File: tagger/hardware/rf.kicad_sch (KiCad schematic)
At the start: 13 parts, among them J3 RADIO_UART, SW1 RADIO_COMMISSION, U7 XB3-24Z8UM-J

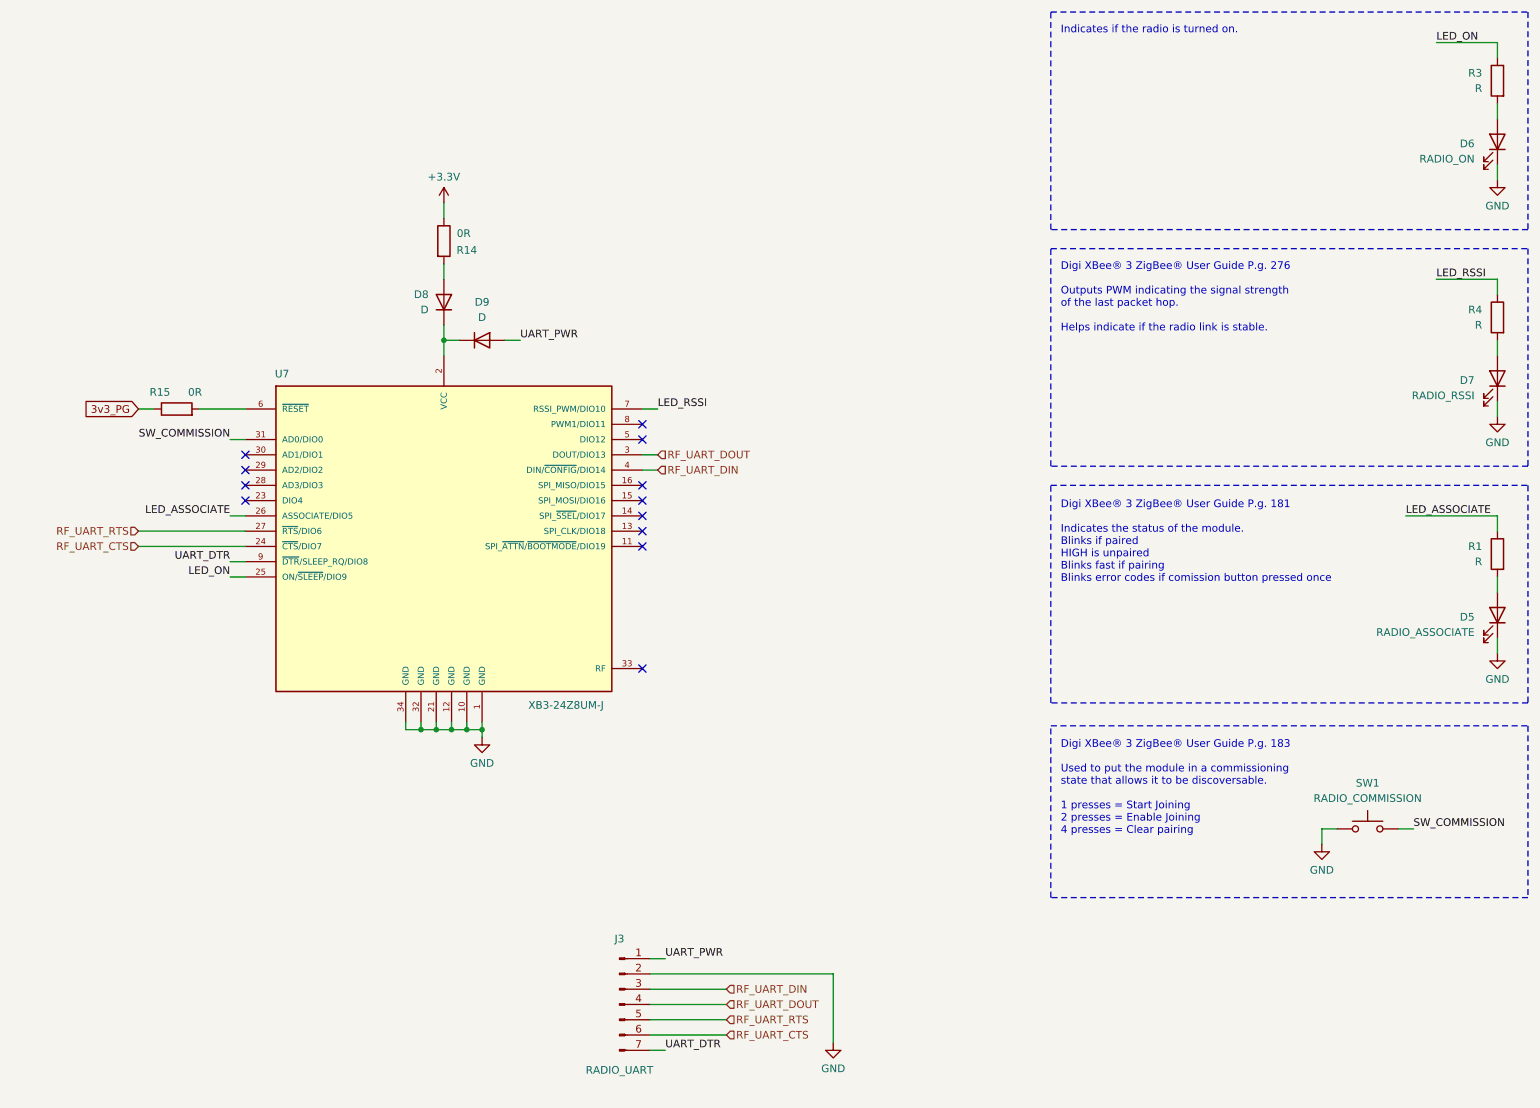
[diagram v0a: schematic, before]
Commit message: feat: schematic organization
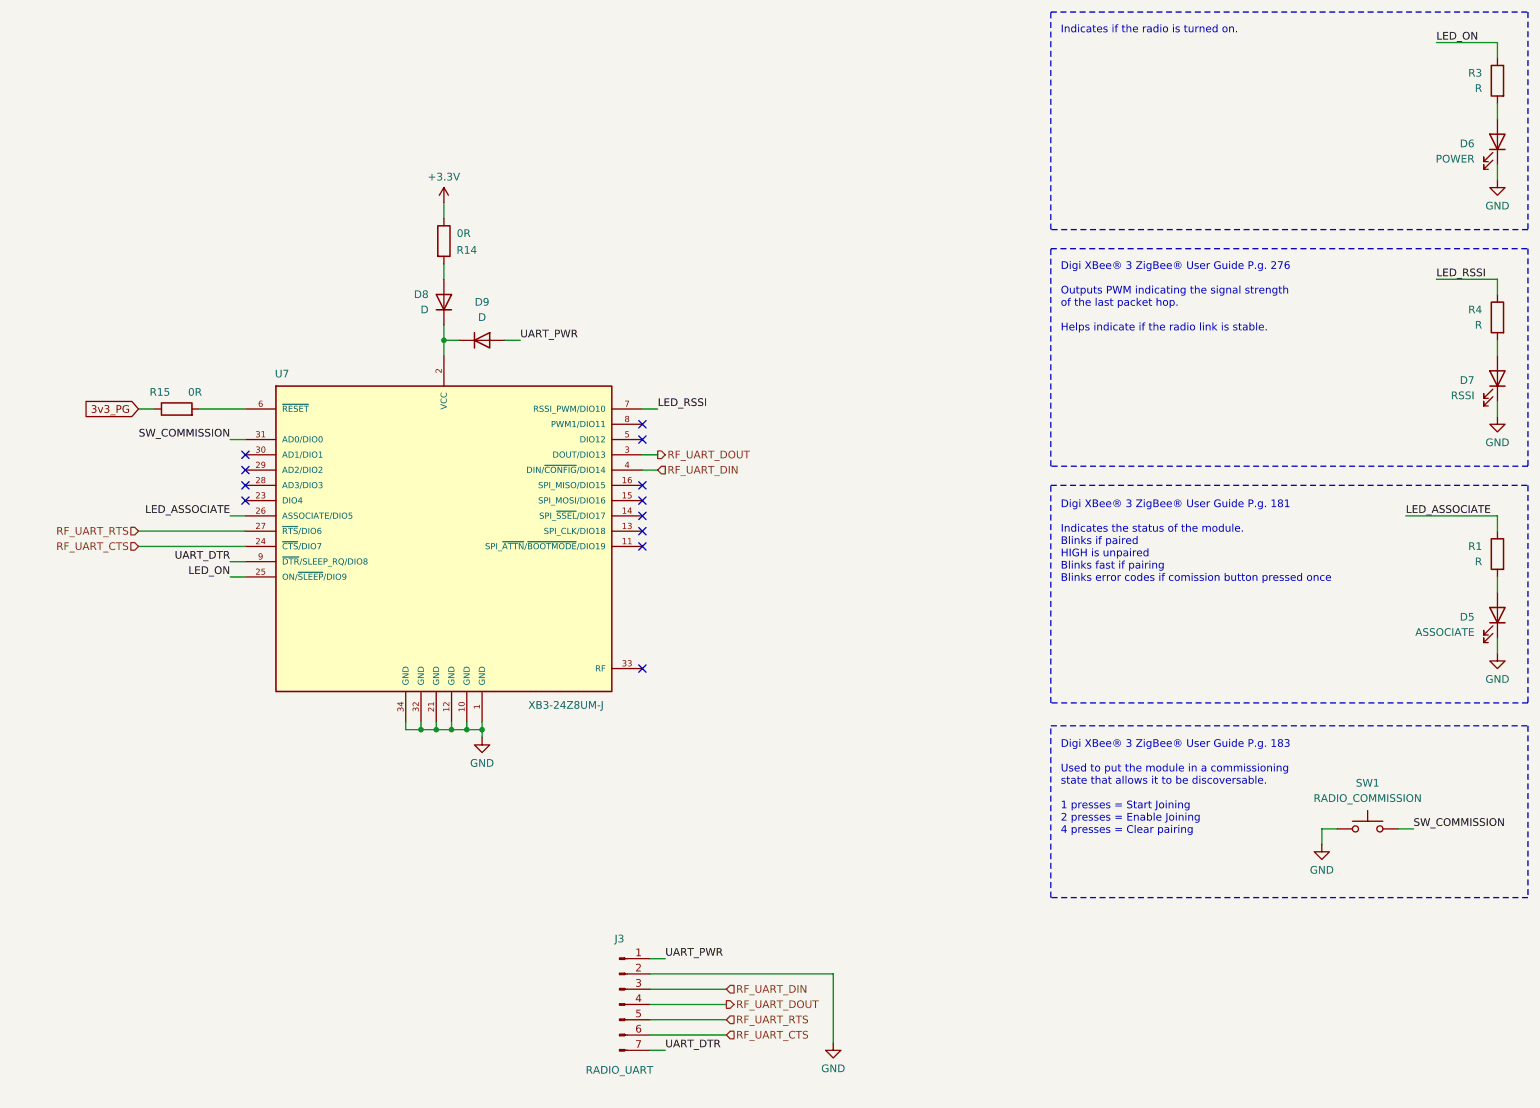
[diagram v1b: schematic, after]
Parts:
- D5: value RADIO_ASSOCIATE -> ASSOCIATE; footprint (none) -> LED_SMD:LED_0603_1608Metric
- D6: value RADIO_ON -> POWER; footprint (none) -> LED_SMD:LED_0603_1608Metric
- D7: value RADIO_RSSI -> RSSI; footprint (none) -> LED_SMD:LED_0603_1608Metric
- R1, R14, R15, R3, R4: footprint (none) -> Resistor_SMD:R_0201_0603Metric_Pad0.64x0.40mm_HandSolder
- SW1: footprint (none) -> Button_Switch_SMD:SW_Push_1P1T_NO_CK_KMR2
- U7: footprint XB3-24Z8UM-J:XCVR_XB3-24Z8UM-J -> RF_XBee:XCVR_XB3-24Z8UM-J
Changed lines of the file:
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@@
 	)
 	(hierarchical_label "RF_UART_DOUT"
-		(shape input)
+		(shape output)
 		(at 148.59 180.34 0)
 		(effects
@@
 	)
 	(hierarchical_label "RF_UART_DOUT"
-		(shape input)
+		(shape output)
 		(at 137.16 88.9 0)
 		(effects
@@
 			)
 		)
-		(property "Value" "RADIO_ASSOCIATE"
+		(property "Value" "ASSOCIATE"
 			(at 273.05 118.4274 90)
 			(effects
@@
 			)
 		)
-		(property "Footprint" ""
+		(property "Footprint" "LED_SMD:LED_0603_1608Metric"
 			(at 276.86 115.57 0)
 			(effects
@@
 			)
 		)
-		(property "Footprint" ""
+		(property "Footprint" "Resistor_SMD:R_0201_0603Metric_Pad0.64x0.40mm_HandSolder"
 			(at 99.822 53.34 90)
 			(effects
@@
 			)
 		)
-		(property "Value" "RADIO_ON"
+		(property "Value" "POWER"
 			(at 273.05 39.6874 90)
 			(effects
@@
 			)
 		)
-		(property "Footprint" ""
+		(property "Footprint" "LED_SMD:LED_0603_1608Metric"
 			(at 276.86 36.83 0)
 			(effects
@@
 			)
 		)
-		(property "Value" "RADIO_RSSI"
+		(property "Value" "RSSI"
 			(at 273.05 79.0574 90)
 			(effects
@@
 			)
 		)
-		(property "Footprint" ""
+		(property "Footprint" "LED_SMD:LED_0603_1608Metric"
 			(at 276.86 76.2 0)
 			(effects
@@
 			)
 		)
-		(property "Footprint" ""
+		(property "Footprint" "Resistor_SMD:R_0201_0603Metric_Pad0.64x0.40mm_HandSolder"
 			(at 57.15 83.058 90)
 			(effects
@@
 			)
 		)
-		(property "Footprint" ""
+		(property "Footprint" "Resistor_SMD:R_0201_0603Metric_Pad0.64x0.40mm_HandSolder"
 			(at 278.638 105.41 90)
 			(effects
@@
 			)
 		)
-		(property "Footprint" "XB3-24Z8UM-J:XCVR_XB3-24Z8UM-J"
+		(property "Footprint" "RF_XBee:XCVR_XB3-24Z8UM-J"
 			(at 101.6 102.87 0)
 			(effects
@@
 			)
 		)
-		(property "Footprint" ""
+		(property "Footprint" "Resistor_SMD:R_0201_0603Metric_Pad0.64x0.40mm_HandSolder"
 			(at 278.638 66.04 90)
 			(effects
@@
 			)
 		)
-		(property "Footprint" ""
+		(property "Footprint" "Button_Switch_SMD:SW_Push_1P1T_NO_CK_KMR2"
 			(at 255.27 146.05 0)
 			(effects
@@
 			)
 		)
-		(property "Footprint" ""
+		(property "Footprint" "Resistor_SMD:R_0201_0603Metric_Pad0.64x0.40mm_HandSolder"
 			(at 278.638 26.67 90)
 			(effects

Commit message: feat: board routing and RS485 implementation
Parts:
- removed J3: RADIO_UART, symbol Connector:Conn_01x07_Pin
- added J1: XBEE_BOOTLOADER, Connector_PinHeader_2.00mm:PinHeader_1x06_P2.00mm_Vertical, symbol Connector:Conn_01x06_Pin
- SW1: value RADIO_COMMISSION -> COMMISSION
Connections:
- net GND: now also J1.2 (Pin_2)
- net RF_UART_DIN: now also J1.3 (Pin_3)
- net RF_UART_DOUT: now also J1.4 (Pin_4)
- net RF_UART_RTS: now also J1.5 (Pin_5)
- net UART_DTR: now also J1.6 (Pin_6)
- net UART_PWR: now also J1.1 (Pin_1)
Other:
- note added: "XBee Bootloader"
- note added: "XBee Bootloader Interface (P.g. 92)"

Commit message: feat: more board layout
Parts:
- added R27: 10k, Resistor_SMD:R_0201_0603Metric_Pad0.64x0.40mm_HandSolder, symbol Device:R
- added SW2: RESET, Button_Switch_SMD:SW_Push_1P1T_NO_CK_KMR2, symbol Switch:SW_Push
- added TP3: TX, TestPoint:TestPoint_Bridge_Pitch2.54mm_Drill1.0mm, symbol Connector:TestPoint
- added TP4: RX, TestPoint:TestPoint_Bridge_Pitch2.54mm_Drill1.0mm, symbol Connector:TestPoint
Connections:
- net +3.3V: now also R27.1
- net GND: now also SW2.1
- net RF_UART_DIN: now also TP4.1
- net RF_UART_DOUT: now also TP3.1
- net 3v3_PG: no longer names the net of R15.1
- net 3v3_PG: now also R27.2, SW2.2

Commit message: feat: various board routing changes
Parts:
- J1: footprint Connector_PinHeader_2.00mm:PinHeader_1x06_P2.00mm_Vertical -> Connector_PinHeader_2.54mm:PinHeader_1x06_P2.54mm_Vertical
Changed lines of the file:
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@@
 			)
 		)
-		(property "Footprint" "Connector_PinHeader_2.00mm:PinHeader_1x06_P2.00mm_Vertical"
+		(property "Footprint" "Connector_PinHeader_2.54mm:PinHeader_1x06_P2.54mm_Vertical"
 			(at 132.08 179.07 0)
 			(effects

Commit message: feat: added missing 3d models
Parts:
- D8, D9: footprint (none) -> Diode_SMD:D_0402_1005Metric
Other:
- note added: "XBee is attatched to UART1 on the STM32 to allow the XBee to re-program the STM32 wirelessly."
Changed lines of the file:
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@@
+		)
+	)
+	(text "XBee is attatched to UART1\non the STM32 to allow the\nXBee to re-program the STM32\nwirelessly."
+		(exclude_from_sim no)
+		(at 155.448 95.25 0)
+		(effects
+			(font
+				(size 1.27 1.27)
+				(color 132 132 132 1)
+			)
+			(justify left top)
 		)
 	)
@@
 	)
 	(junction
+		(at 149.86 173.99)
+		(diameter 0)
+		(color 0 0 0 0)
+	)
+	(junction
 		(at 107.95 134.62)
 		(diameter 0)
@@
 	(wire
 		(pts
+			(xy 149.86 173.99) (xy 137.16 173.99)
+		)
+		(stroke
+			(width 0)
+			(type default)
+		)
+	)
+	(wire
+		(pts
 			(xy 261.62 99.06) (xy 276.86 99.06)
 		)
@@
 	(wire
 		(pts
+			(xy 149.86 172.72) (xy 149.86 173.99)
+		)
+		(stroke
+			(width 0)
+			(type default)
+		)
+	)
+	(wire
+		(pts
 			(xy 137.16 186.69) (xy 139.7 186.69)
 		)
@@
 	(wire
 		(pts
-			(xy 139.7 173.99) (xy 137.16 173.99)
+			(xy 151.13 173.99) (xy 149.86 173.99)
 		)
 		(stroke
@@
 	)
 	(label "UART_PWR"
-		(at 139.7 173.99 0)
+		(at 151.13 173.99 0)
 		(effects
 			(font
@@
 			)
 		)
-		(property "Footprint" ""
+		(property "Footprint" "Diode_SMD:D_0402_1005Metric"
 			(at 107.95 69.85 0)
 			(effects
@@
 	)
 	(symbol
+		(lib_id "power:PWR_FLAG")
+		(at 149.86 172.72 0)
+		(unit 1)
+		(exclude_from_sim no)
+		(in_bom yes)
+		(on_board yes)
+		(dnp no)
+		(property "Reference" "#FLG03"
+			(at 149.86 170.815 0)
+			(effects
+				(font
+					(size 1.27 1.27)
+				)
+				(hide yes)
+			)
+		)
+		(property "Value" "PWR_FLAG"
+			(at 149.86 168.402 0)
+			(effects
+				(font
+					(size 1.27 1.27)
+				)
+			)
+		)
+		(property "Footprint" ""
+			(at 149.86 172.72 0)
+			(effects
+				(font
+					(size 1.27 1.27)
+				)
+				(hide yes)
+			)
+		)
+		(property "Datasheet" "~"
+			(at 149.86 172.72 0)
+			(effects
+				(font
+					(size 1.27 1.27)
+				)
+				(hide yes)
+			)
+		)
+		(property "Description" "Special symbol for telling ERC where power comes from"
+			(at 149.86 172.72 0)
+			(effects
+				(font
+					(size 1.27 1.27)
+				)
+				(hide yes)
+			)
+		)
+		(pin "1"
+		)
+		(instances
+			(project ""
+				(path "/7f9981c1-8446-4881-979b-6d88a629918c/b67527ae-871d-46f9-8cb4-d3003ac65ae8"
+					(reference "#FLG03")
+					(unit 1)
+				)
+			)
+		)
+	)
+	(symbol
 		(lib_id "power:+3.3V")
 		(at 49.53 67.31 0)
@@
 			)
 		)
-		(property "Footprint" ""
+		(property "Footprint" "Diode_SMD:D_0402_1005Metric"
 			(at 101.6 63.5 0)
 			(effects

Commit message: feat: schematic organization, added SD card connections
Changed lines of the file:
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@@
+	(wire
+		(pts
+			(xy 99.06 69.85) (xy 101.6 69.85)
+		)
+		(stroke
+			(width 0)
+			(type default)
+		)
+	)
 	(wire
 		(pts
@@
 					(unit 1)
 				)
+			)
+		)
+	)
+	(symbol
+		(lib_id "power:PWR_FLAG")
+		(at 99.06 69.85 90)
+		(unit 1)
+		(exclude_from_sim no)
+		(in_bom yes)
+		(on_board yes)
+		(dnp no)
+		(property "Reference" "#FLG04"
+			(at 97.155 69.85 0)
+			(effects
+				(font
+					(size 1.27 1.27)
+				)
+				(hide yes)
+			)
+		)
+		(property "Value" "PWR_FLAG"
+			(at 94.742 69.85 0)
+			(effects
+				(font
+					(size 1.27 1.27)
+				)
+			)
+		)
+		(property "Footprint" ""
+			(at 99.06 69.85 0)
+			(effects
+				(font
+					(size 1.27 1.27)
+				)
+				(hide yes)
+			)
+		)
+		(property "Datasheet" "~"
+			(at 99.06 69.85 0)
+			(effects
+				(font
+					(size 1.27 1.27)
+				)
+				(hide yes)
+			)
+		)
+		(property "Description" "Special symbol for telling ERC where power comes from"
+			(at 99.06 69.85 0)
+			(effects
+				(font
+					(size 1.27 1.27)
+				)
+				(hide yes)
+			)
+		)
+		(pin "1"
+		)
+		(instances
+			(project "tagger"
+				(path "/7f9981c1-8446-4881-979b-6d88a629918c/b67527ae-871d-46f9-8cb4-d3003ac65ae8"
+					(reference "#FLG04")
+					(unit 1)
+				)

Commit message: feat: replace RS485 transceiver, fix DRC warnings
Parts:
- removed J1: XBEE_BOOTLOADER, Connector_PinHeader_2.54mm:PinHeader_1x06_P2.54mm_Vertical, symbol Connector:Conn_01x06_Pin
- added TP10: DTR, TestPoint:TestPoint_Pad_D1.0mm, symbol Connector:TestPoint
- added TP8: 3v3, TestPoint:TestPoint_Pad_D1.0mm, symbol Connector:TestPoint
- added TP9: RTS, TestPoint:TestPoint_Pad_D1.0mm, symbol Connector:TestPoint
- D6: value POWER -> PWR
- R1, R14, R15, R27, R3, R4: footprint Resistor_SMD:R_0201_0603Metric_Pad0.64x0.40mm_HandSolder -> Resistor_SMD:R_0402_1005Metric
- SW1: value COMMISSION -> COMM
- U7: now not fitted
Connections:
- net RF_UART_RTS: now also TP9.1
- net UART_DTR: now also TP10.1
- net UART_PWR: no longer names the net of D9.2 (A)
- net UART_PWR: now also TP8.1
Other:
- note removed: "XBee Bootloader"
